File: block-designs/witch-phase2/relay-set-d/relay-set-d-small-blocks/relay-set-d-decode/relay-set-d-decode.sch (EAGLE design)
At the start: 67 parts, among them IC1 74LS138D, IC13 74LVC1G125DBV, IC14 74LVC1G125DBV, IC15 74LVC1G125DBV, IC16 74LVC1G125DBV, IC17 74LVC1G125DBV, IC18 74LVC1G125DBV, IC19 74LVC1G125DBV, IC2 74LS138D, IC20 74LVC1G125DBV, IC21 74LVC1G125DBV, IC22 74LVC1G125DBV, IC3 74LS138D, IC4 74LS138D

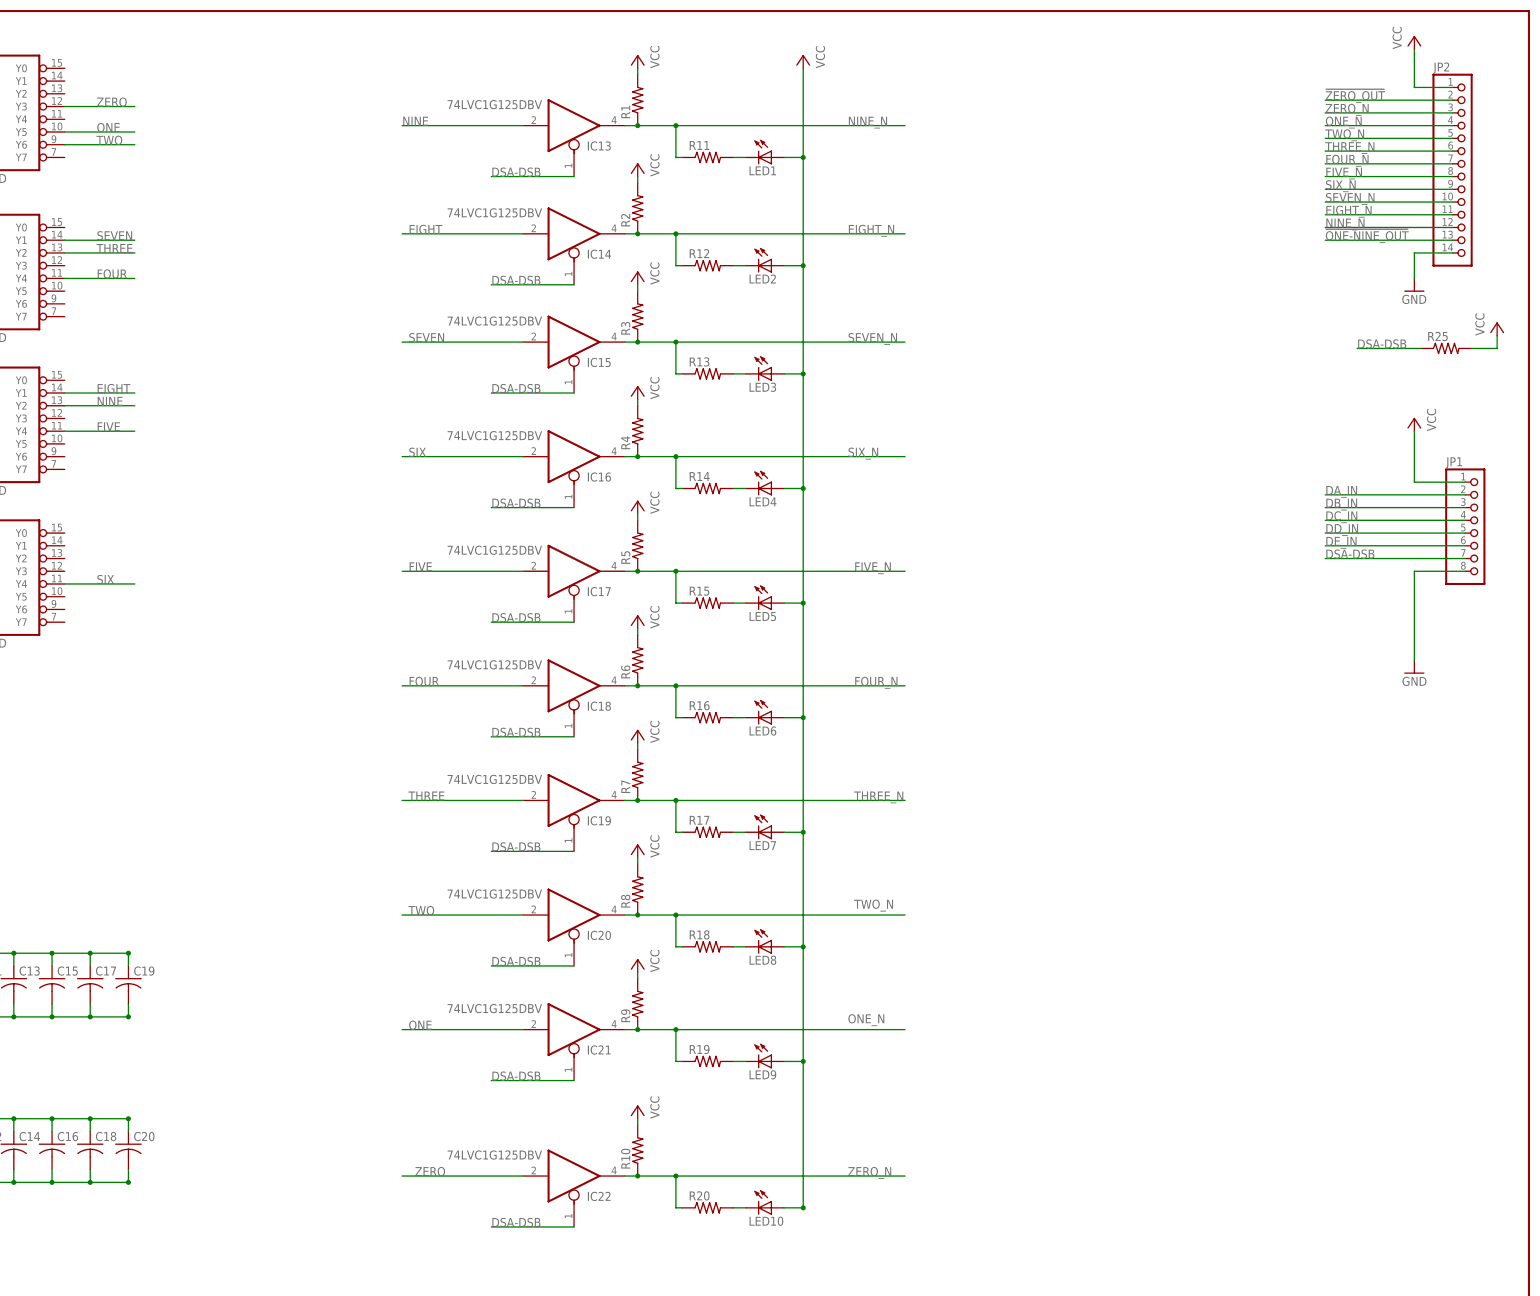
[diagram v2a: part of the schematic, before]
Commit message: updated layout for easy interface to the rest of the system
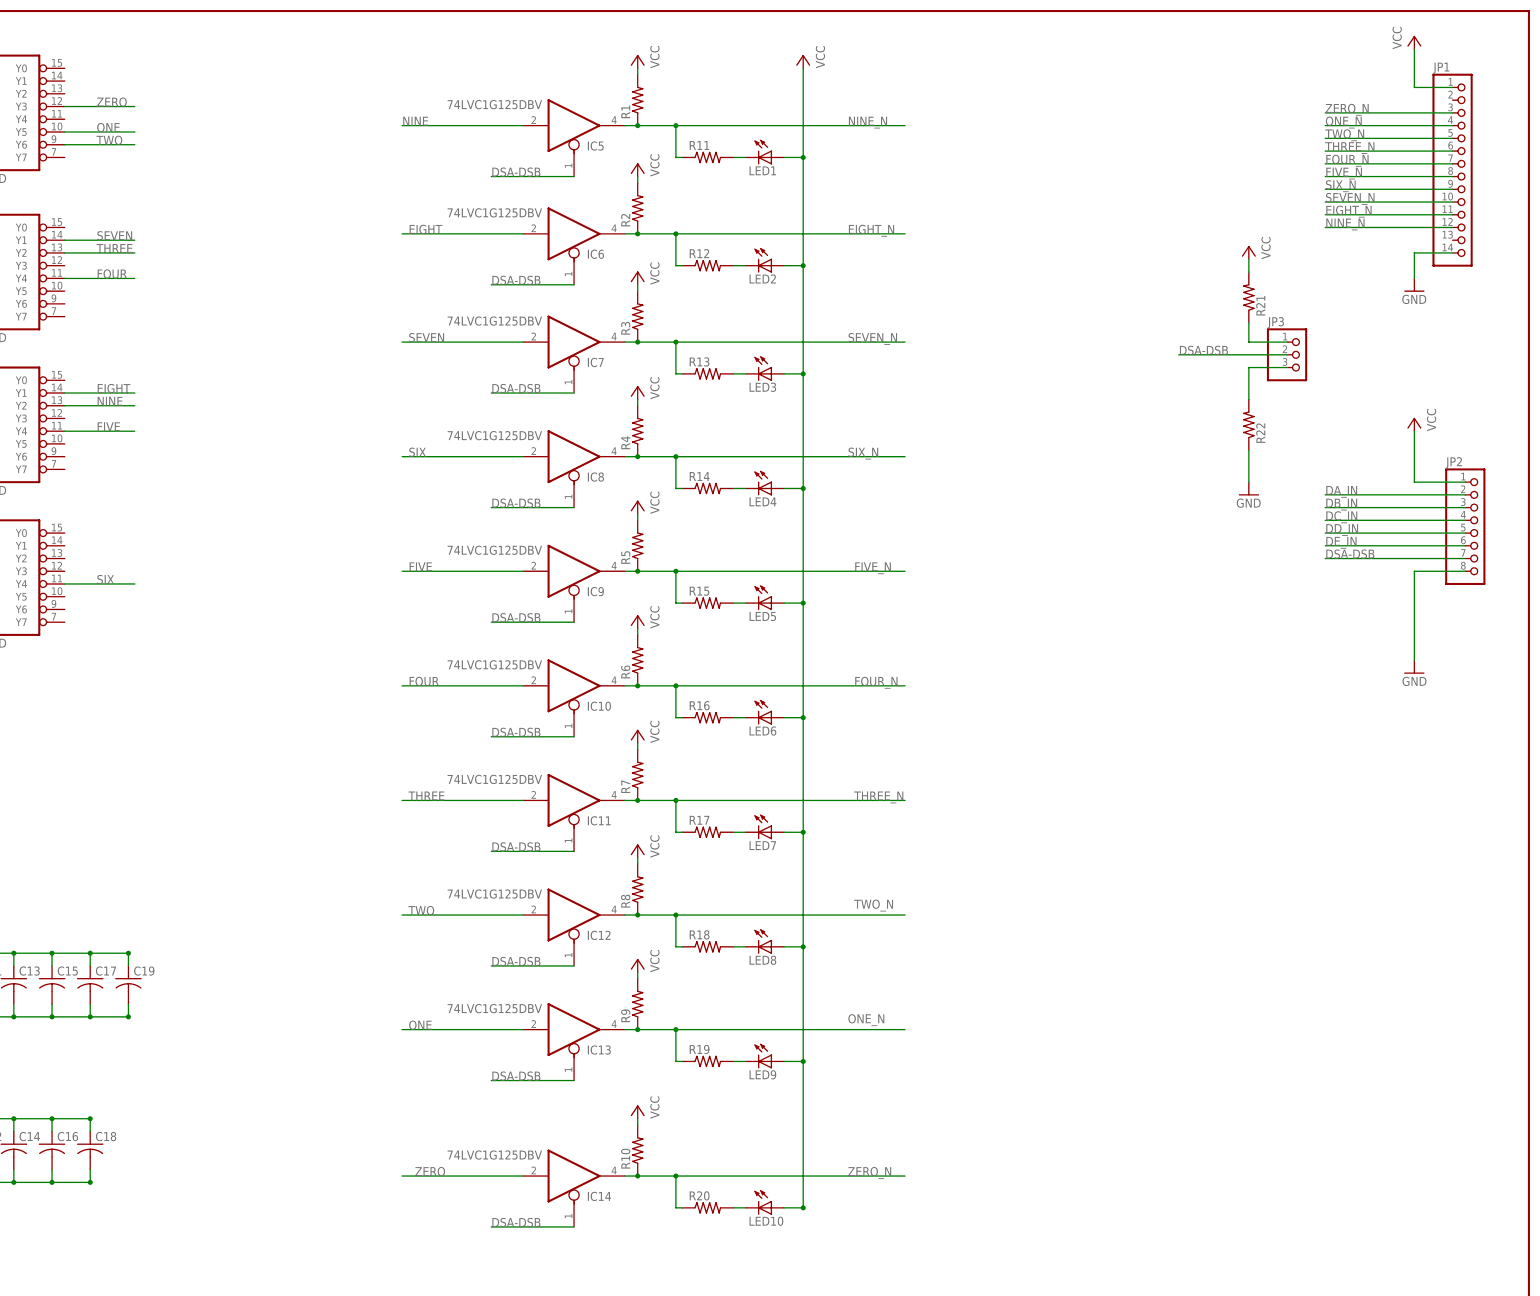
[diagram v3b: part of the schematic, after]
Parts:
- removed C20: (no value), resistor:C-USC0805
- removed IC21, IC22: 74LVC1G125DBV, 74xx-little-us:74LVC1G125DBV
- removed R25: (no value), resistor:R-US_R0805
- added IC5, IC6: 74LVC1G125DBV, 74xx-little-us:74LVC1G125DBV
- added JP3: (no value), pinhead:PINHD-1X3
- added R21, R22: (no value), resistor:R-US_R0805
- JP1: device pinhead:PINHD-1X8 -> pinhead:PINHD-1X14
- JP2: device pinhead:PINHD-1X14 -> pinhead:PINHD-1X8
- renumbered IC15 to IC7, IC16 to IC8, IC17 to IC9, IC18 to IC10, IC19 to IC11, IC20 to IC12
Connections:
- removed net !ONE-NINE_OUT: JP2.13
- removed net !ZERO_OUT: JP2.2
- new net N$11: JP3.1, R21.1
- new net N$13: JP3.3, R22.2
- net DA_IN: now also JP2.2; no longer JP1.2
- net DB_IN: now also JP2.3; no longer JP1.3
- net DC_IN: now also JP2.4; no longer JP1.4
- net DD_IN: now also JP2.5; no longer JP1.5
- net DE_IN: now also JP2.6; no longer JP1.6
- net DSA-DSB: now also IC5A.OE, IC6A.OE, JP2.7, JP3.2; no longer IC21A.OE, IC22A.OE, JP1.7, R25.1
- net EIGHT: now also IC6A.I; no longer IC14A.I
- net EIGHT_N: now also IC6A.O, JP1.11; no longer IC14A.O, JP2.11
- net FIVE_N: now also JP1.8; no longer JP2.8
- net FOUR_N: now also JP1.7; no longer JP2.7
- net GND: now also JP1.14, JP2.8, R22.1; no longer C20.2, JP1.8, JP2.14
- net NINE: now also IC5A.I; no longer IC13A.I
- net NINE_N: now also IC5A.O, JP1.12; no longer IC13A.O, JP2.12
- net ONE: now also IC13A.I; no longer IC21A.I
- net ONE_N: now also IC13A.O, JP1.4; no longer IC21A.O, JP2.4
- net SEVEN_N: now also JP1.10; no longer JP2.10
- net SIX_N: now also JP1.9; no longer JP2.9
- net THREE_N: now also JP1.6; no longer JP2.6
- net TWO_N: now also JP1.5; no longer JP2.5
- net VCC: now also R21.2; no longer C20.1, R25.2
- net ZERO: now also IC14A.I; no longer IC22A.I
- net ZERO_N: now also IC14A.O, JP1.3; no longer IC22A.O, JP2.3
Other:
- moved on the sheet: IC13, IC14

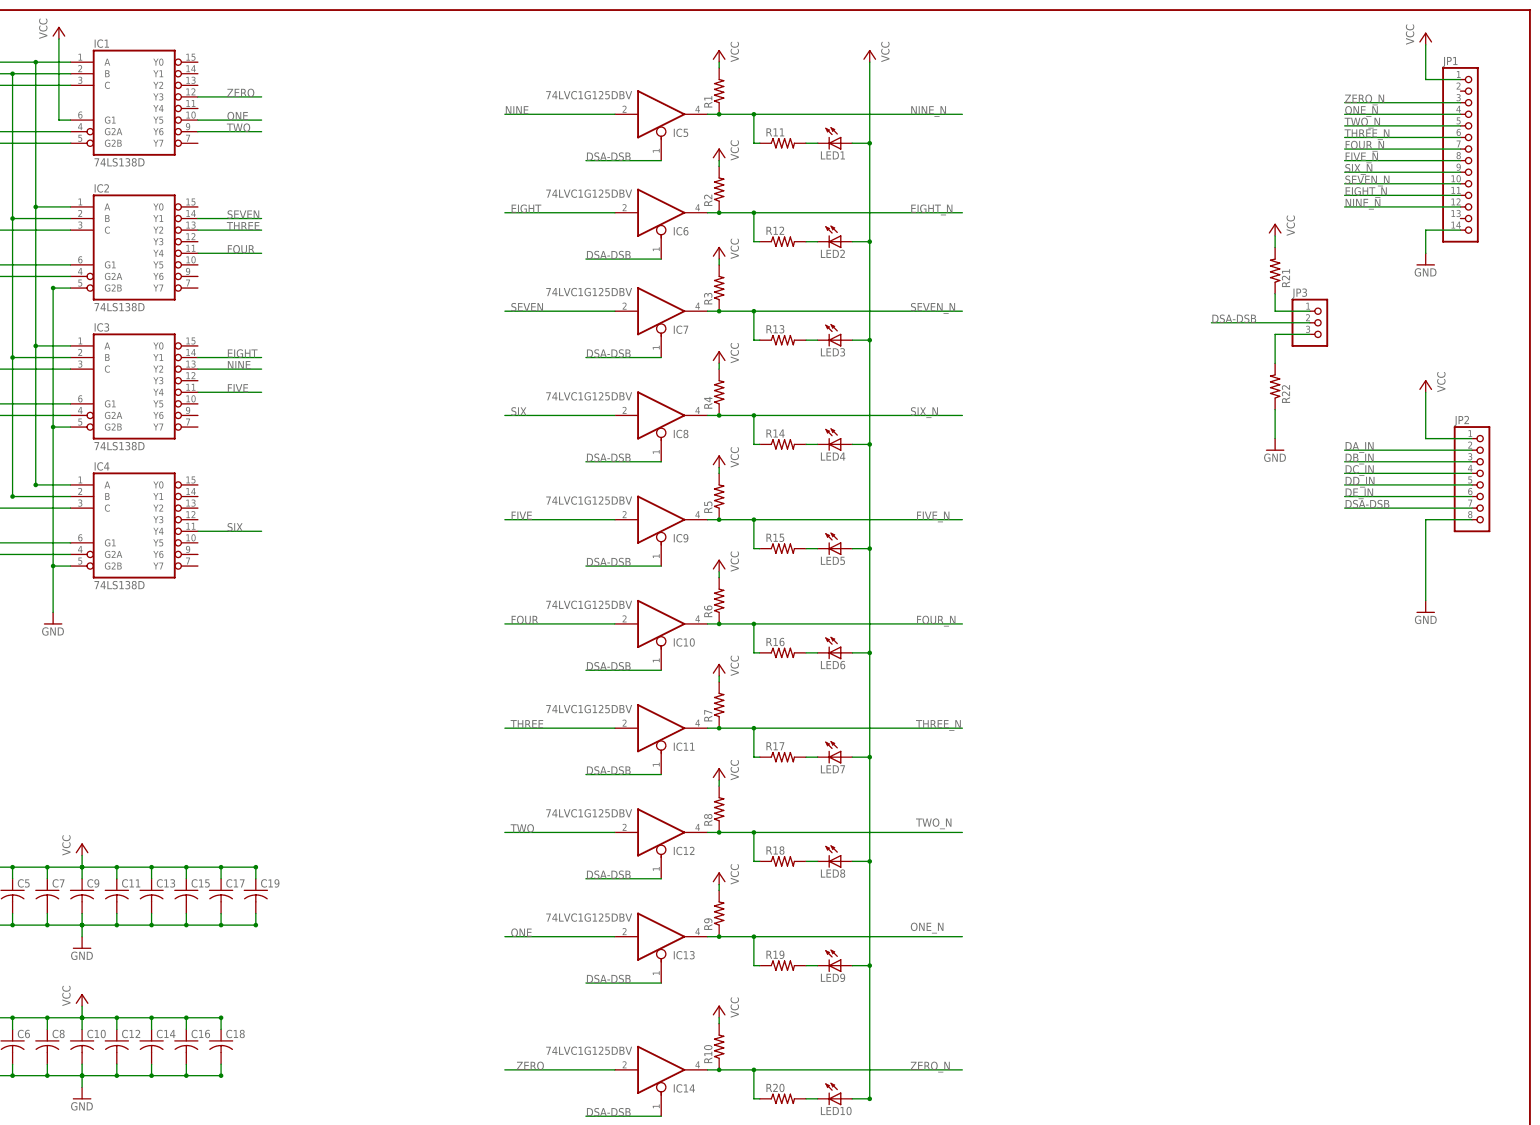
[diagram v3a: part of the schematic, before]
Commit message: change 0.1uF caps from 0805 to 0603
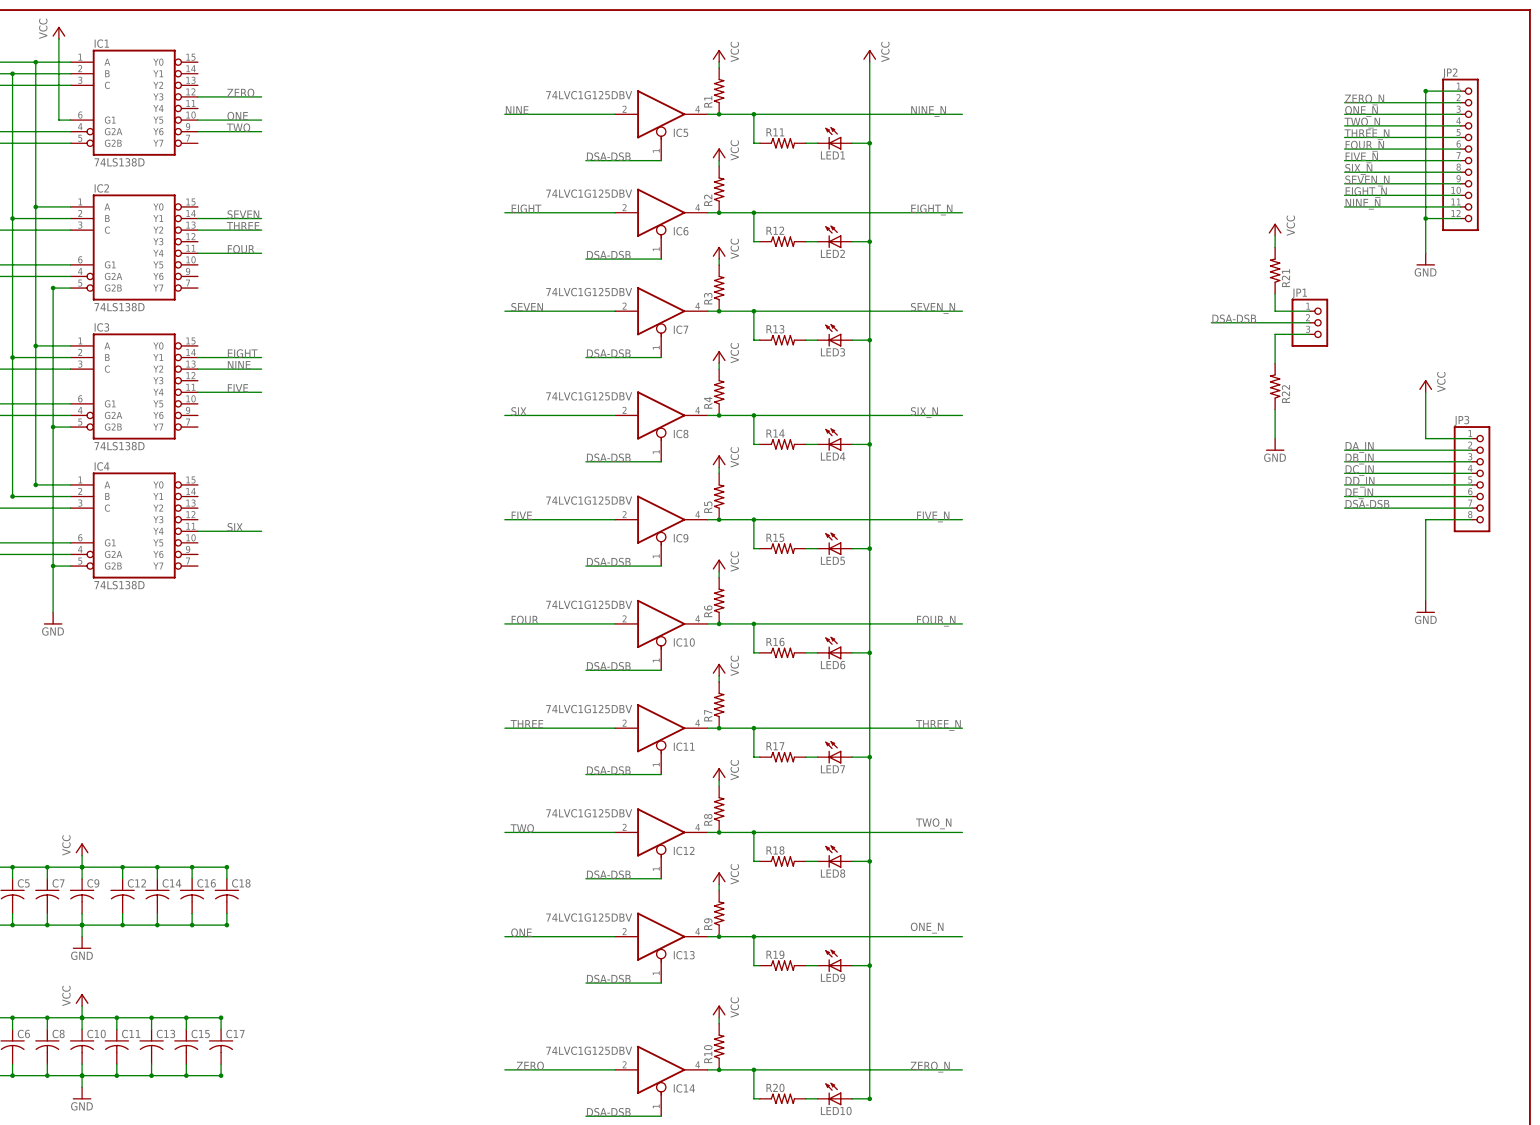
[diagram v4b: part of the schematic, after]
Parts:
- removed C19: (no value), resistor:C-USC0805
- C1, C10, C11, C12, C13, C14, C15, C16, C17, C18, C2, C3, C4, C6, C8: device resistor:C-USC0805 -> resistor:C-USC0603
- JP1: device pinhead:PINHD-1X14 -> pinhead:PINHD-1X3
- JP2: device pinhead:PINHD-1X8 -> custom-pinhead:PINHD-1X12
- JP3: device pinhead:PINHD-1X3 -> pinhead:PINHD-1X8
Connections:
- net DA_IN: now also JP3.2; no longer JP2.2
- net DB_IN: now also JP3.3; no longer JP2.3
- net DC_IN: now also JP3.4; no longer JP2.4
- net DD_IN: now also JP3.5; no longer JP2.5
- net DE_IN: now also JP3.6; no longer JP2.6
- net DSA-DSB: now also JP1.2, JP3.7; no longer JP2.7, JP3.2
- net EIGHT_N: now also JP2.10; no longer JP1.11
- net FIVE_N: now also JP2.7; no longer JP1.8
- net FOUR_N: now also JP2.6; no longer JP1.7
- net GND: now also JP2.1, JP2.12, JP3.8; no longer C19.2, JP1.14, JP2.8
- net N$11: now also JP1.1; no longer JP3.1
- net N$13: now also JP1.3; no longer JP3.3
- net NINE_N: now also JP2.11; no longer JP1.12
- net ONE_N: now also JP2.3; no longer JP1.4
- net SEVEN_N: now also JP2.9; no longer JP1.10
- net SIX_N: now also JP2.8; no longer JP1.9
- net THREE_N: now also JP2.5; no longer JP1.6
- net TWO_N: now also JP2.4; no longer JP1.5
- net VCC: now also JP3.1; no longer C19.1, JP1.1, JP2.1
- net ZERO_N: now also JP2.2; no longer JP1.3
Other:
- moved on the sheet: C11, C12, C13, C14, C15, C16, C17, C18
